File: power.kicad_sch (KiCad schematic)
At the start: 47 parts, among them Q301 BSC014N04LS, SW301 228ADS2, U301 LTC2955CTS8-1, U302 PAC1954, U303 LTC4231-2, U304 AP64501SP-13

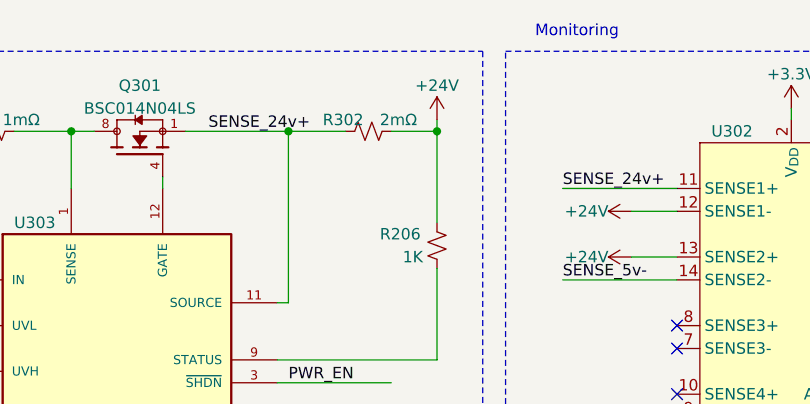
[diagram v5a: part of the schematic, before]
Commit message: Fix the 24v sense res and the IR port MPN.
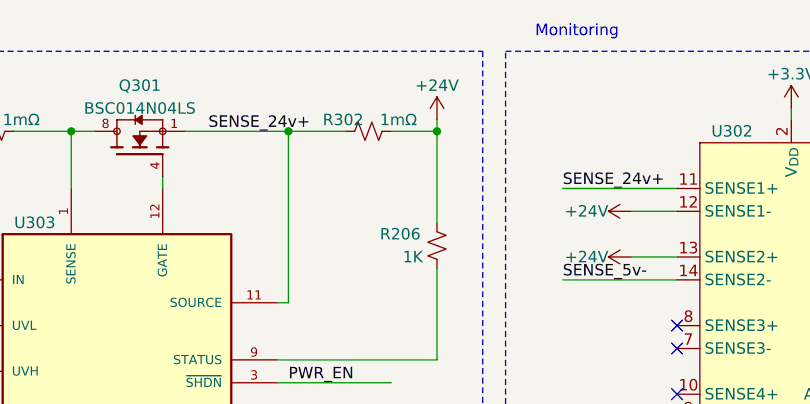
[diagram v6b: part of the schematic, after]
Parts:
- R302: value 2mΩ -> 1mΩ; MPN PEWF2512F2L00Q9 -> EBWM2512F1L00S9
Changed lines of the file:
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@@
       (effects (font (size 1.27 1.27)) (justify left))
     )
-    (property "Value" "2mΩ" (at 168.91 27.94 90)
+    (property "Value" "1mΩ" (at 168.91 27.94 90)
       (effects (font (size 1.27 1.27)) (justify left))
     )
@@
       (effects (font (size 1.27 1.27)) hide)
     )
-    (property "MPN" "PEWF2512F2L00Q9" (at 167.64 29.21 0)
+    (property "MPN" "EBWM2512F1L00S9" (at 167.64 29.21 0)
       (effects (font (size 1.27 1.27)) hide)
     )
